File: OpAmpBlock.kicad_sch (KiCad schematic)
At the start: 23 parts, among them SW1 SW_SPST, SW2 SW_SPST, SW23 SW_DIP_x08, SW3 SW_Push_DPDT, SW4 SW_SPST, SW6 SW_Rotary_1x4_MP, SW7 SW_SP3T, SW8 SW_SPST, SW9 SW_SPST, U1 OPA992

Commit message: minor schematic changes, 4 way dip now used instead of 6. switch and pot footprints and symbols done
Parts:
- removed C1, C2: C_Polarized, symbol Device:C_Polarized
- removed C3, C4, C5: C, symbol Device:C
- removed SW1, SW2, SW4, SW8, SW9: SW_SPST, symbol Switch:SW_SPST
- removed SW23: SW_DIP_x08, symbol Switch:SW_DIP_x08
- removed SW6: SW_Rotary_1x4_MP, symbol Switch:SW_Rotary_1x4_MP
- removed U1: OPA992, Package_TO_SOT_SMD:SOT-23-5_HandSoldering, symbol uniOpAmpLib:OPA992
- added C32, C33, C34, C35: C, Capacitor_SMD:C_0805_2012Metric_Pad1.18x1.45mm_HandSolder, symbol Device:C
- added SW2: 218-8LPSTR, uniOpAmpLib:218-8LPSTR, symbol uniOpAmpLib:218-8LPSTR
- added SW3: CS-4-14, uniOpAmpLib:CS-4-14NB, symbol uniOpAmpLib:CS-4-14
- added SW5: 218-6LPSTR, uniOpAmpLib:218-6LPSTR, symbol uniOpAmpLib:218-6LPSTR
- added SW8: SW_Push_DPDT, uniOpAmpLib:CAS-DxxB, symbol Switch:SW_Push_DPDT
- added U1: OPA992DBV, Package_TO_SOT_SMD:SOT-23-5_HandSoldering, symbol uniOpAmpLib:OPA992DBV
- C10: footprint (none) -> uniOpAmpLib:F461_8-2uf
- C6, C8: footprint (none) -> Capacitor_SMD:C_0805_2012Metric_Pad1.18x1.45mm_HandSolder
- C7, C9: footprint (none) -> uniOpAmpLib:PP_CAP
- D1: value D -> 1N4148WS
- RV1, RV2: footprint (none) -> uniOpAmpLib:PVG5H
- SW10: renamed from SW7; footprint (none) -> uniOpAmpLib:CS-4-13NB
- SW7: renamed from SW3; footprint (none) -> uniOpAmpLib:CAS-DxxB
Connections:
- net +VDC: now also C8.1, C34.1, C35.1, U1.5 (V+)
- net -VDC: now also C32.2, C33.2, U1.2 (V-)
- net 1A: now also SW2.16
- net 2A: now also SW2.15
- net 3A: now also SW2.14
- net 4A: now also SW2.13
- net 5A: now also SW2.12
- net 6A: now also SW2.11
- net 7A: now also SW2.10
- net 8A: now also SW2.9
- net A: now also SW2.1, SW2.2, SW2.3, SW2.4, SW2.5, SW2.6, SW2.7, SW2.8, SW5.10 (O), SW5.11 (O)
- net GND: now also C8.2, C32.1, C33.1, C34.2, C35.2, SW5.2 (I), SW5.6 (I)
- net N: now also SW5.12 (O), SW8.5 (B); no longer C8.1
- net at D1.2 (A): now also SW5.5 (I), U1.1
- net at RV2.2: now also SW8.1 (A), U1.3 (+)
- net at RV1.2: now also SW8.3 (C), U1.4 (-)
- net at SW7.2 (B): now also C10.1, C7.1, C9.1, SW3.1, SW8.6 (C); no longer RV2.1
- net at SW7.3 (C), SW7.4 (A): now also SW5.8 (O)
- net at RV1.3: now also SW5.4 (I)
- net at RV1.1: now also SW8.4 (A); no longer C8.2
- net at C10.2: now also SW3.4
- net at C9.2: now also SW3.3
- net at C7.2: now also SW3.2
- new net: SW3.C, SW8.2 (B)
- new net: RV2.1, SW7.5 (B)
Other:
- note added: "use remaining SPST switch for either additional diff. capacitor or for reverse diode"
- moved on the sheet: C10, C6, C7, C9, RV1, RV2, SW10, SW7

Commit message: Initial PCB layout
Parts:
- removed SW10: SW_SP3T, uniOpAmpLib:CS-4-13NB, symbol Switch:SW_SP3T
- removed SW5: 218-6LPSTR, uniOpAmpLib:218-6LPSTR, symbol uniOpAmpLib:218-6LPSTR
- added SW3: 218-4LPSTR, uniOpAmpLib:218-4LPSTR, symbol uniOpAmpLib:218-4LPSTR
- added SW7: SW_SP3T, uniOpAmpLib:CS-4-13NB, symbol uniOpAmpLib:SW_SP3T
- C1: renamed from C34; footprint Capacitor_SMD:C_0805_2012Metric_Pad1.18x1.45mm_HandSolder -> uniOpAmpLib:C_0805_Metric2012_HandSolder
- C2: renamed from C32; footprint Capacitor_SMD:C_0805_2012Metric_Pad1.18x1.45mm_HandSolder -> uniOpAmpLib:C_0805_Metric2012_HandSolder
- C3: renamed from C35; footprint Capacitor_SMD:C_0805_2012Metric_Pad1.18x1.45mm_HandSolder -> uniOpAmpLib:C_0805_Metric2012_HandSolder
- C4: renamed from C33; footprint Capacitor_SMD:C_0805_2012Metric_Pad1.18x1.45mm_HandSolder -> uniOpAmpLib:C_0805_Metric2012_HandSolder
- C5: renamed from C8; footprint Capacitor_SMD:C_0805_2012Metric_Pad1.18x1.45mm_HandSolder -> uniOpAmpLib:C_0805_Metric2012_HandSolder
- C6: footprint Capacitor_SMD:C_0805_2012Metric_Pad1.18x1.45mm_HandSolder -> uniOpAmpLib:C_0805_Metric2012_HandSolder
- C9: renamed from C10; footprint uniOpAmpLib:F461_8-2uf -> uniOpAmpLib:PP_CAP
- D1: footprint (none) -> Diode_SMD:D_SOD-323
- SW4: renamed from SW7; value SW_Push_DPDT -> SW_DPDT
- SW5: renamed from SW8; value SW_Push_DPDT -> SW_DPDT
- U1: footprint Package_TO_SOT_SMD:SOT-23-5_HandSoldering -> uniOpAmpLib:SOT-23-5_HandSoldering
- renumbered C9 to C8, SW3 to SW6, SW2 to SW8
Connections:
- net A: now also SW3.3 (I), SW3.4 (I), SW7.3 (4)
- net GND: now also SW3.1 (I), SW3.2 (I), SW7.1
- net N: now also SW3.5 (O)
- net at D1.2 (A), U1.1: now also SW3.8 (O)
- net at SW4.3 (C), SW4.4 (A): now also SW3.6 (O)
- net at RV1.3: now also SW3.7 (O)
- net at RV2.3: now also SW7.C
- no-connect marks 0 -> 1
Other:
- note removed: "use remaining SPST switch for either additional diff. capacitor or for reverse diode"
- moved on the sheet: C7, C8, C9, D1

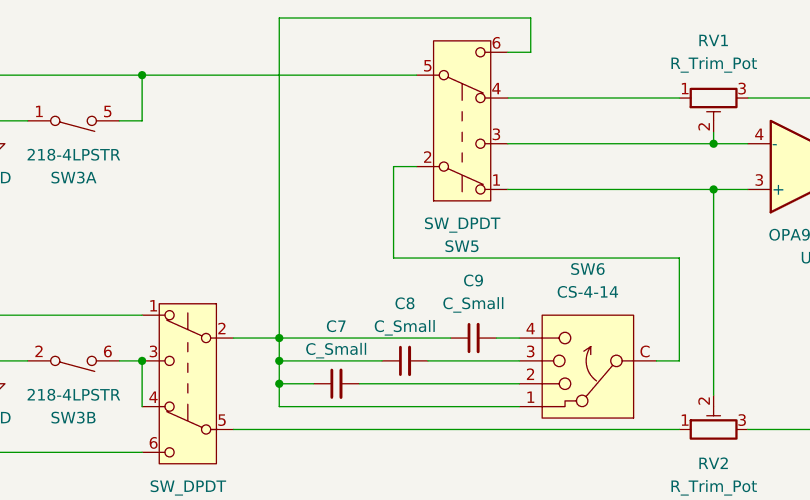
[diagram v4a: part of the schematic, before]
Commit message: Voltage controlled current output circuit and preliminary layout added
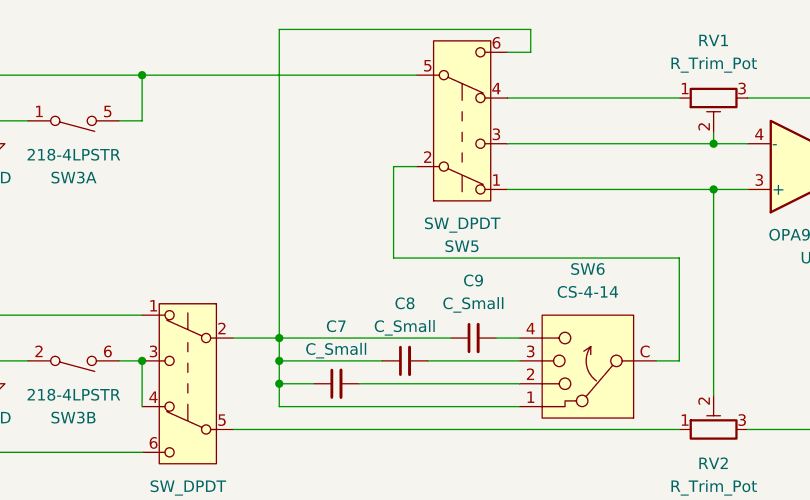
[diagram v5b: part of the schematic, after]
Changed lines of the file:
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@@
 	(wire
 		(pts
-			(xy 140.97 64.77) (xy 113.03 64.77)
+			(xy 140.97 66.04) (xy 113.03 66.04)
 		)
 		(stroke
@@
 	(wire
 		(pts
-			(xy 113.03 64.77) (xy 113.03 100.33)
+			(xy 113.03 66.04) (xy 113.03 100.33)
 		)
 		(stroke
@@
 	(wire
 		(pts
-			(xy 140.97 68.58) (xy 140.97 64.77)
-		)
-		(stroke
+			(xy 140.97 68.58) (xy 140.97 66.04)
+		)
+		(stroke
